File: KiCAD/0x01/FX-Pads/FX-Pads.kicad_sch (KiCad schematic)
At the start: 36 parts, among them J1 CONTROL, J2 DATA, SW1 SW_Push, SW10 SW_Push, SW11 SW_Push, SW12 SW_Push, SW13 SW_Push, SW14 SW_Push, SW15 SW_Push, SW16 SW_Push, SW2 SW_Push, SW3 SW_Push, SW4 SW_Push, SW5 SW_Push, SW6 SW_Push, SW7 SW_Push, SW8 SW_Push, SW9 SW_Push, U1 CD74HC4067M

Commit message: pads
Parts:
- added H1, H10, H11, H12, H13, H14, H15, H16, H2, H3, H4, H5, H6, H7, H8, H9: MountingHole, MountingHole:MountingHole_2mm, symbol Mechanical:MountingHole

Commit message: fx pads gerbers
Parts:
- added H17, H18, H19, H20: MountingHole, MountingHole:MountingHole_2.2mm_M2, symbol Mechanical:MountingHole
- H1, H10, H11, H12, H13, H14, H15, H16, H2, H3, H4, H5, H6, H7, H8, H9: footprint MountingHole:MountingHole_2mm -> MountingHole:MountingHole_3.2mm_M3_ISO7380
- R1: footprint PCM_Resistor_SMD_AKL:R_0805_2012Metric_Pad1.20x1.40mm_HandSolder -> Resistor_SMD:R_0805_2012Metric_Pad1.20x1.40mm_HandSolder

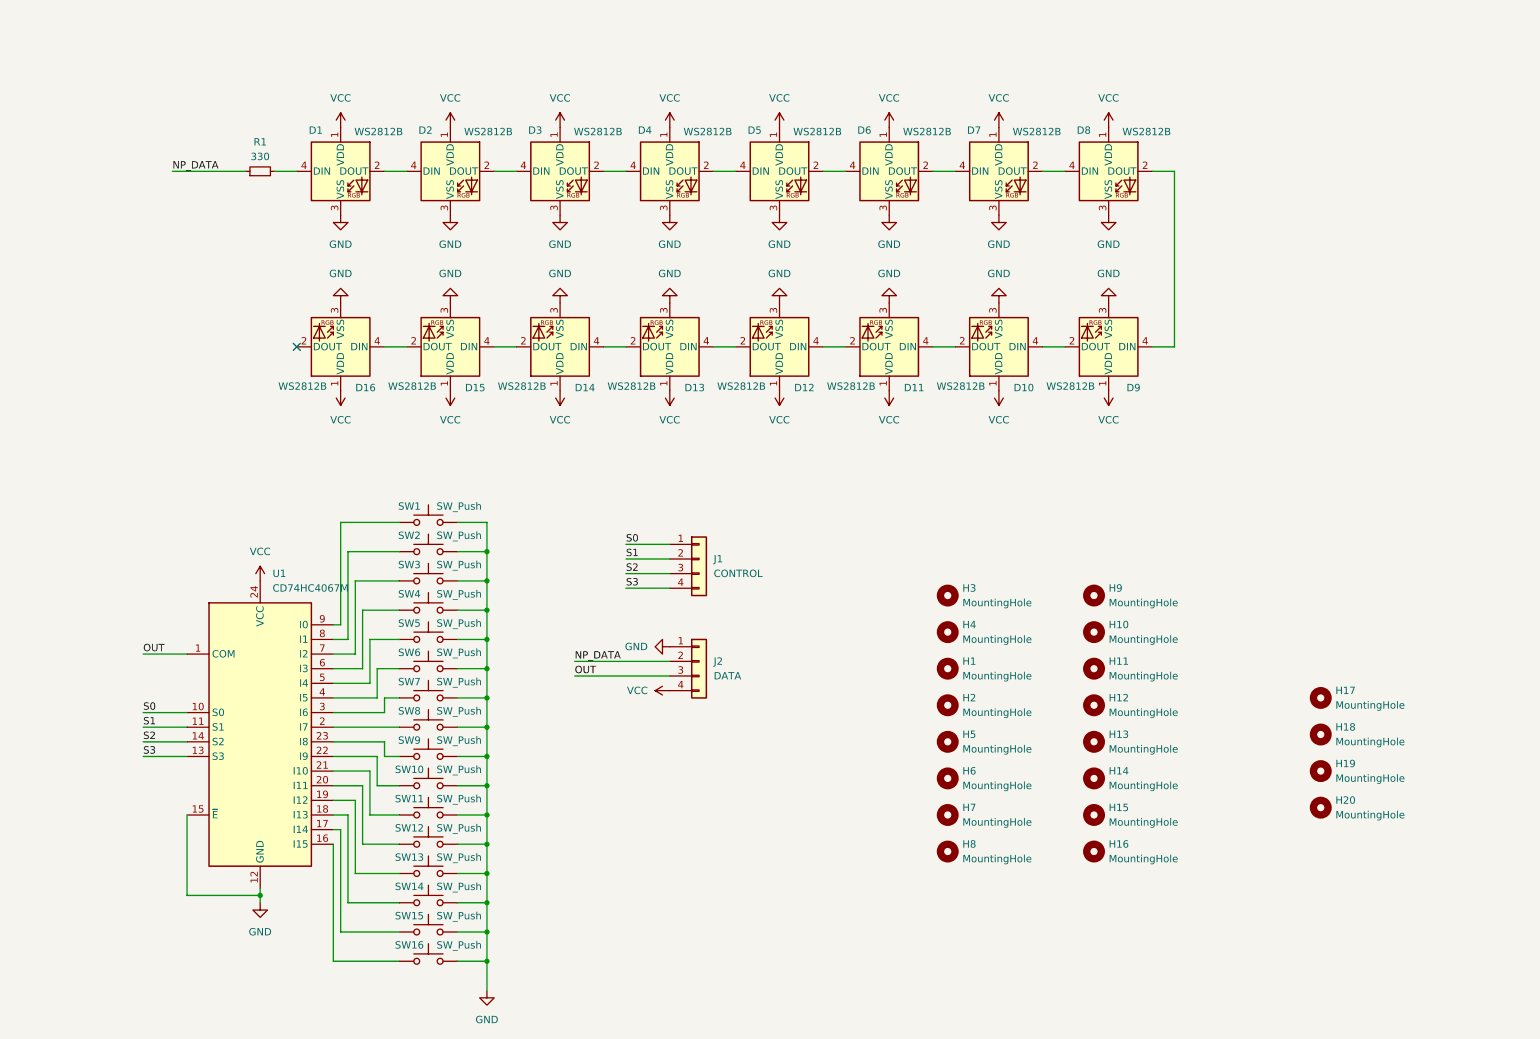
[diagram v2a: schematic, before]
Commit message: fx-pads routing
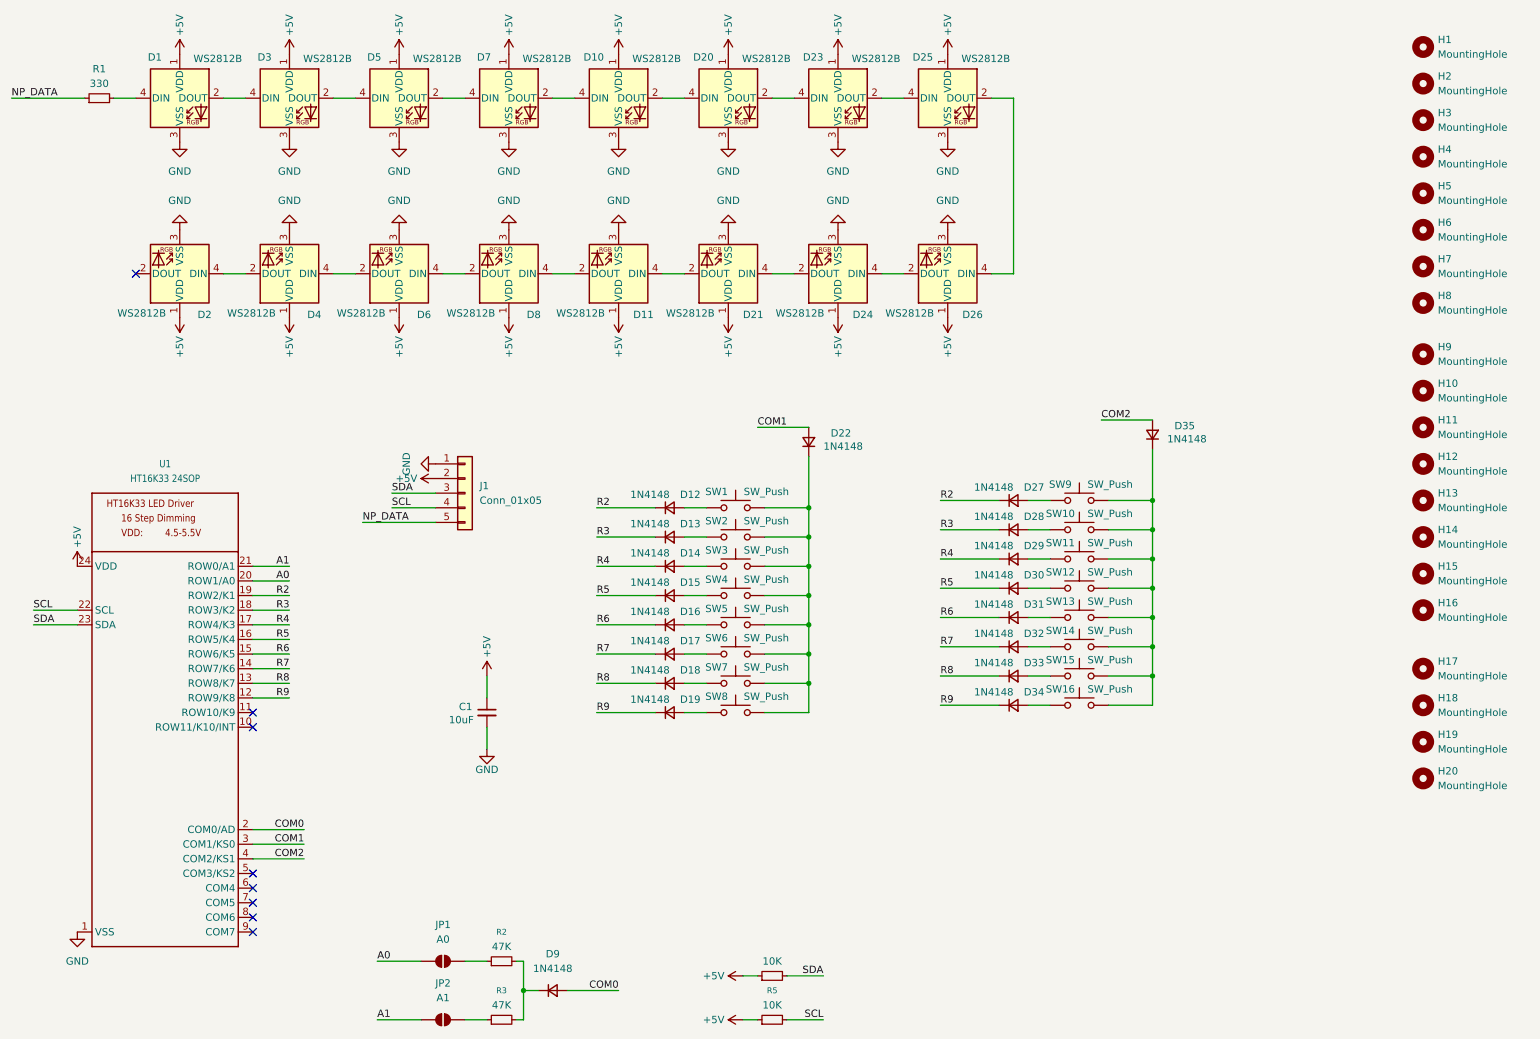
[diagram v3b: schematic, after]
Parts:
- removed J1: CONTROL, Connector_PinHeader_2.54mm:PinHeader_1x04_P2.54mm_Vertical, symbol Connector_Generic:Conn_01x04
- removed J2: DATA, Connector_PinHeader_2.54mm:PinHeader_1x04_P2.54mm_Vertical, symbol Connector_Generic:Conn_01x04
- removed U1: CD74HC4067M, Package_SO:SOIC-24W_7.5x15.4mm_P1.27mm, symbol 74xx:CD74HC4067M
- added C1: 10uF, Capacitor_SMD:C_0805_2012Metric_Pad1.18x1.45mm_HandSolder, symbol Device:C_Small
- added D12, D13, D14, D15, D16, D17, D18, D19, D22, D27, D28, D29, D30, D31, D32, D33, D34, D35: 1N4148, Diode_SMD:D_SOD-123, symbol Device:D_Small
- added D9: 1N4148, Diode_SMD:D_SOD-323_HandSoldering, symbol Device:D_Small
- added J1: Conn_01x05, Connector_JST:JST_PH_S5B-PH-K_1x05_P2.00mm_Horizontal, symbol Connector_Generic:Conn_01x05
- added JP1: A0, Jumper:SolderJumper-2_P1.3mm_Open_RoundedPad1.0x1.5mm, symbol Jumper:SolderJumper_2_Open
- added JP2: A1, Jumper:SolderJumper-2_P1.3mm_Open_RoundedPad1.0x1.5mm, symbol Jumper:SolderJumper_2_Open
- added R2, R3: 47K, Resistor_SMD:R_0805_2012Metric_Pad1.20x1.40mm_HandSolder, symbol Device:R_Small
- added R4, R5: 10K, Resistor_SMD:R_0805_2012Metric_Pad1.20x1.40mm_HandSolder, symbol Device:R_Small
- added U1: HT16K33 24SOP, Package_SO:SOIC-24W_7.5x15.4mm_P1.27mm, symbol ht16k33_sop28:HT16K33_SOP24
- renumbered D5 to D10, D12 to D11, D16 to D2, D6 to D20, D11 to D21, D7 to D23, D10 to D24, D8 to D25, D9 to D26, D2 to D3, D15 to D4, D3 to D5, D14 to D6, D4 to D7, D13 to D8, H3 to H1, H4 to H2, H1 to H3, H2 to H4
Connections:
- net GND: now also C1.2, J1.1 (Pin_1), U1.1 (VSS); no longer SW1.2, SW10.2, SW11.2, SW12.2, SW13.2, SW14.2, SW15.2, SW16.2, SW2.2, SW3.2, SW4.2, SW5.2, SW6.2, SW7.2, SW8.2, SW9.2
- net NP_DATA: now also J1.5 (Pin_5)
- net at SW7.1: now also D18.2 (A)
- net at SW5.1: now also D16.2 (A)
- net at SW1.1: now also D12.2 (A)
- net at SW2.1: now also D13.2 (A)
- net at SW4.1: now also D15.2 (A)
- net at SW12.1: now also D30.2 (A)
- net at SW3.1: now also D14.2 (A)
- net at SW13.1: now also D31.2 (A)
- net at SW8.1: now also D19.2 (A)
- net at SW11.1: now also D29.2 (A)
- net at SW6.1: now also D17.2 (A)
- net at SW15.1: now also D33.2 (A)
- net at SW14.1: now also D32.2 (A)
- net at SW10.1: now also D28.2 (A)
- net at SW16.1: now also D34.2 (A)
- net at SW9.1: now also D27.2 (A)
- net VCC renamed +5V
- net +5V: now also C1.1, J1.2 (Pin_2), R4.1, R5.1, U1.24 (VDD)
- new net: D22.1 (K), SW1.2, SW2.2, SW3.2, SW4.2, SW5.2, SW6.2, SW7.2, SW8.2
- new net: JP2.2 (B), R3.1
- new net: JP1.2 (B), R2.1
- new net: D9.1 (K), R2.2, R3.2
- new net: D35.1 (K), SW10.2, SW11.2, SW12.2, SW13.2, SW14.2, SW15.2, SW16.2, SW9.2
- new net A0: JP1.1 (A), U1.20 (ROW1/A0)
- new net A1: JP2.1 (A), U1.21 (ROW0/A1)
- new net COM0: D9.2 (A), U1.2 (COM0/AD)
- new net COM1: D22.2 (A), U1.3 (COM1/KS0)
- new net COM2: D35.2 (A), U1.4 (COM2/KS1)
- new net R2: D12.1 (K), D27.1 (K), U1.19 (ROW2/K1)
- new net R3: D13.1 (K), D28.1 (K), U1.18 (ROW3/K2)
- new net R4: D14.1 (K), D29.1 (K), U1.17 (ROW4/K3)
- new net R5: D15.1 (K), D30.1 (K), U1.16 (ROW5/K4)
- new net R6: D16.1 (K), D31.1 (K), U1.15 (ROW6/K5)
- new net R7: D17.1 (K), D32.1 (K), U1.14 (ROW7/K6)
- new net R8: D18.1 (K), D33.1 (K), U1.13 (ROW8/K7)
- new net R9: D19.1 (K), D34.1 (K), U1.12 (ROW9/K8)
- new net SCL: J1.4 (Pin_4), R5.2, U1.22 (SCL)
- new net SDA: J1.3 (Pin_3), R4.2, U1.23 (SDA)
- no-connect marks 1 -> 8
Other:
- moved on the sheet: D1, D10, D11, D2, D20, D21, D23, D24, D25, D26, D3, D4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

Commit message: micropython
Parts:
- added C2, C3, C4, C5, C6, C7, C8, C9: 1uF, Capacitor_SMD:C_0603_1608Metric_Pad1.08x0.95mm_HandSolder, symbol Device:C_Small
- D9: footprint Diode_SMD:D_SOD-323_HandSoldering -> Diode_SMD:D_SOD-123
- renumbered D20 to D12, D21 to D13, D23 to D14, D24 to D15, D25 to D16, D26 to D17, D27 to D18, D28 to D19, D29 to D20, D30 to D21, D31 to D22, D32 to D23, D33 to D24, D34 to D25, D12 to D26, D13 to D27, D14 to D28, D15 to D29, D16 to D30, D17 to D31, D18 to D32, D19 to D33, D35 to D34, D22 to D35, SW9 to SW1, SW2 to SW10, SW3 to SW11, SW4 to SW12, SW5 to SW13, SW6 to SW14, SW7 to SW15, SW8 to SW16, SW10 to SW2, SW11 to SW3, SW12 to SW4, SW13 to SW5, SW14 to SW6, SW15 to SW7, SW16 to SW8, SW1 to SW9
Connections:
- net +5V: now also C2.1, C3.1, C4.1, C5.1, C6.1, C7.1, C8.1, C9.1
- net GND: now also C2.2, C3.2, C4.2, C5.2, C6.2, C7.2, C8.2, C9.2
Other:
- moved on the sheet: C1, D18, D19, D20, D21, D22, D23, D24, D25, D26, D27, D28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
